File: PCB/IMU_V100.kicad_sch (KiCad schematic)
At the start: 0 parts

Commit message: Updated PCB
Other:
- sheet Barometer ports: added CLK_BMP280, MISO_BMP280, MOSI_BMP280, nCSS_BMP280; removed none
- sheet MCU ports: added CLK_BMP280, MISO_BMP280, MOSI_BMP280, nCSS_BMP280; removed none
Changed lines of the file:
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@@
+	(wire
+		(pts
+			(xy 165.1 140.97) (xy 231.14 140.97)
+		)
+		(stroke
+			(width 0)
+			(type default)
+		)
+	)
 	(wire
 		(pts
@@
 	(wire
 		(pts
+			(xy 165.1 143.51) (xy 231.14 143.51)
+		)
+		(stroke
+			(width 0)
+			(type default)
+		)
+	)
+	(wire
+		(pts
 			(xy 78.74 55.88) (xy 78.74 116.84)
 		)
@@
 	(wire
 		(pts
+			(xy 165.1 138.43) (xy 231.14 138.43)
+		)
+		(stroke
+			(width 0)
+			(type default)
+		)
+	)
+	(wire
+		(pts
 			(xy 49.53 35.56) (xy 99.06 35.56)
 		)
@@
 	(wire
 		(pts
+			(xy 90.17 166.37) (xy 113.03 166.37)
+		)
+		(stroke
+			(width 0)
+			(type default)
+		)
+	)
+	(wire
+		(pts
 			(xy 81.28 114.3) (xy 113.03 114.3)
 		)
@@
 	(wire
 		(pts
+			(xy 82.55 158.75) (xy 113.03 158.75)
+		)
+		(stroke
+			(width 0)
+			(type default)
+		)
+	)
+	(wire
+		(pts
+			(xy 52.07 163.83) (xy 82.55 163.83)
+		)
+		(stroke
+			(width 0)
+			(type default)
+		)
+	)
+	(wire
+		(pts
 			(xy 63.5 133.35) (xy 113.03 133.35)
 		)
@@
 	(wire
 		(pts
+			(xy 85.09 161.29) (xy 113.03 161.29)
+		)
+		(stroke
+			(width 0)
+			(type default)
+		)
+	)
+	(wire
+		(pts
 			(xy 68.58 95.25) (xy 68.58 128.27)
 		)
@@
 	(wire
 		(pts
+			(xy 87.63 168.91) (xy 87.63 163.83)
+		)
+		(stroke
+			(width 0)
+			(type default)
+		)
+	)
+	(wire
+		(pts
+			(xy 52.07 171.45) (xy 90.17 171.45)
+		)
+		(stroke
+			(width 0)
+			(type default)
+		)
+	)
+	(wire
+		(pts
+			(xy 82.55 163.83) (xy 82.55 158.75)
+		)
+		(stroke
+			(width 0)
+			(type default)
+		)
+	)
+	(wire
+		(pts
 			(xy 139.7 13.97) (xy 139.7 39.37)
 		)
@@
 	(wire
 		(pts
+			(xy 87.63 163.83) (xy 113.03 163.83)
+		)
+		(stroke
+			(width 0)
+			(type default)
+		)
+	)
+	(wire
+		(pts
+			(xy 85.09 166.37) (xy 85.09 161.29)
+		)
+		(stroke
+			(width 0)
+			(type default)
+		)
+	)
+	(wire
+		(pts
 			(xy 101.6 93.98) (xy 113.03 93.98)
 		)
@@
 		(pts
 			(xy 49.53 55.88) (xy 78.74 55.88)
+		)
+		(stroke
+			(width 0)
+			(type default)
+		)
+	)
+	(wire
+		(pts
+			(xy 90.17 171.45) (xy 90.17 166.37)
+		)
+		(stroke
+			(width 0)
+			(type default)
+		)
+	)
+	(wire
+		(pts
+			(xy 52.07 168.91) (xy 87.63 168.91)
+		)
+		(stroke
+			(width 0)
+			(type default)
+		)
+	)
+	(wire
+		(pts
+			(xy 52.07 166.37) (xy 85.09 166.37)
 		)
 		(stroke
@@
 			)
 		)
+		(pin "nCSS_BMP280" input
+			(at 52.07 163.83 0)
+			(effects
+				(font
+					(size 1.27 1.27)
+				)
+				(justify right)
+			)
+		)
+		(pin "MOSI_BMP280" input
+			(at 52.07 171.45 0)
+			(effects
+				(font
+					(size 1.27 1.27)
+				)
+				(justify right)
+			)
+		)
+		(pin "MISO_BMP280" output
+			(at 52.07 168.91 0)
+			(effects
+				(font
+					(size 1.27 1.27)
+				)
+				(justify right)
+			)
+		)
+		(pin "CLK_BMP280" input
+			(at 52.07 166.37 0)
+			(effects
+				(font
+					(size 1.27 1.27)
+				)
+				(justify right)
+			)
+		)
 		(instances
 			(project "IMU_V100"
@@
 		)
 		(pin "CAN_RX" input
-			(at 165.1 139.7 0)
+			(at 165.1 138.43 0)
 			(effects
 				(font
@@
 		)
 		(pin "CAN_TX" output
-			(at 165.1 142.24 0)
+			(at 165.1 140.97 0)
 			(effects
 				(font
@@
 		)
 		(pin "CAN_SHUTDOWN" output
-			(at 165.1 144.78 0)
+			(at 165.1 143.51 0)
 			(effects
 				(font
@@
 			)
 		)
+		(pin "MISO_BMP280" input
+			(at 113.03 163.83 180)
+			(effects
+				(font
+					(size 1.27 1.27)
+				)
+				(justify left)
+			)
+		)
+		(pin "MOSI_BMP280" output
+			(at 113.03 166.37 180)
+			(effects
+				(font
+					(size 1.27 1.27)
+				)
+				(justify left)
+			)
+		)
+		(pin "nCSS_BMP280" output
+			(at 113.03 158.75 180)
+			(effects
+				(font
+					(size 1.27 1.27)
+				)
+				(justify left)
+			)
+		)
+		(pin "CLK_BMP280" output
+			(at 113.03 161.29 180)
+			(effects
+				(font
+					(size 1.27 1.27)
+				)
+				(justify left)
+			)
+		)

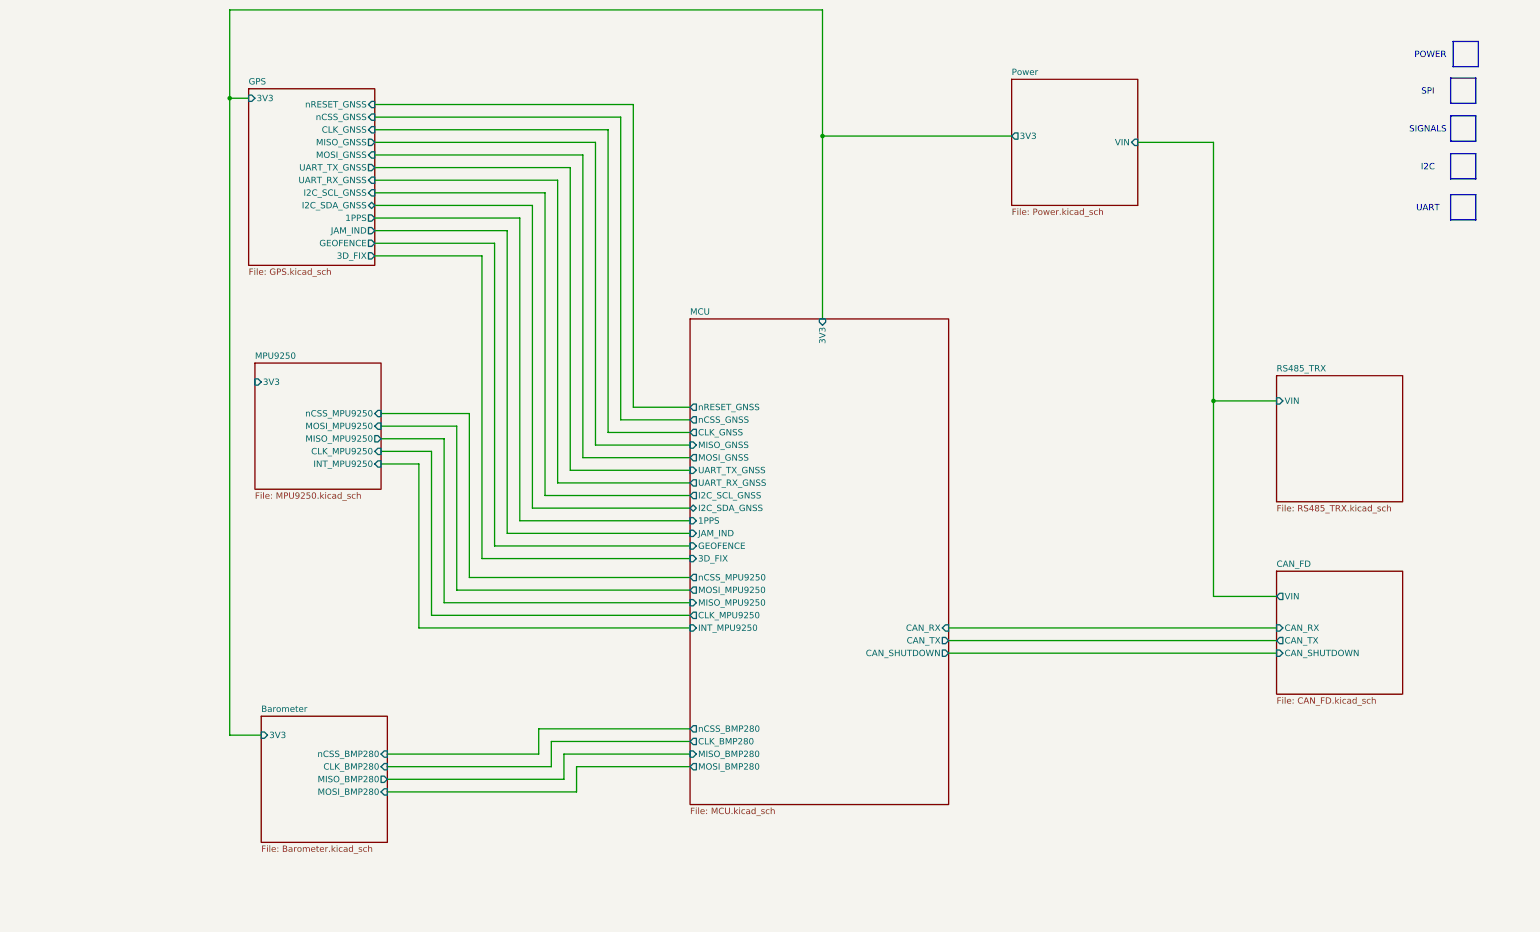
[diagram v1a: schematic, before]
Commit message: Updated PCB. Added Debug section and rectifed RS485
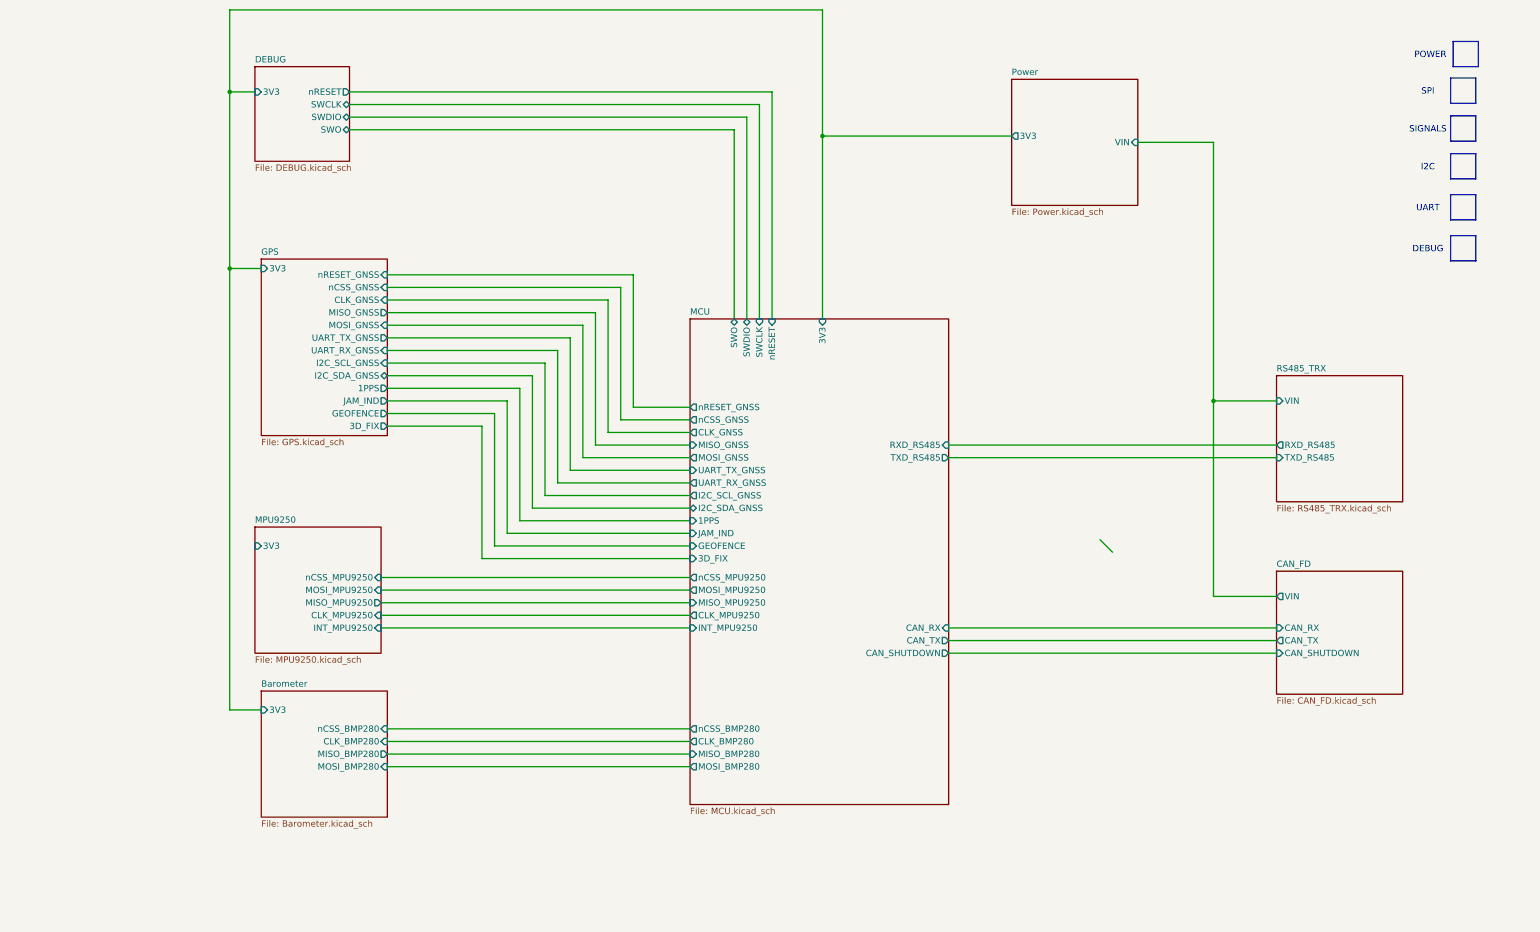
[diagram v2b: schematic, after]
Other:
- added sheet DEBUG (DEBUG.kicad_sch)
- sheet MCU ports: added RXD_RS485, SWCLK, SWDIO, SWO, TXD_RS485, nRESET; removed none
- sheet RS485_TRX ports: added RXD_RS485, TXD_RS485; removed none
- note added: "DEBUG"

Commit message: Updated PCB.
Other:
- removed sheet Barometer
- removed sheet CAN_FD
- removed sheet DEBUG
- removed sheet GPS
- removed sheet MCU
- removed sheet MPU9250
- removed sheet Power
- removed sheet RS485_TRX
- added sheet Block_Diagram (Block_Diagram.kicad_sch)
- added sheet Project_Architecture (Project_Architecture.kicad_sch)
- note added: "1"
- note added: "2"
- note added: "2/10/2024"
- note added: "3"
- note added: "4"
- note added: "Barometer"
- note added: "Block Diagram"
- note added: "Index"
- note added: "Innertial Measurement Unit"
- note added: "Main Page"
- note added: "Page"
- note added: "Poject Architecture"
- note added: "REV 1.0.0"
- note removed: "DEBUG"
- note removed: "I2C"
- note removed: "POWER"
- note removed: "SIGNALS"
- note removed: "SPI"
- note removed: "UART"

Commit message: Updated PCB.
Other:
- note added: "10"
- note added: "11"
- note added: "5"
- note added: "6"
- note added: "7"
- note added: "8"
- note added: "9"
- note added: "CAN FD"
- note added: "DEBUG"
- note added: "DESIGN NOTES"
- note added: "GPS"
- note added: "MCU"
- note added: "MPU9250"
- note added: "Power"
- note added: "RS485 TRX"
